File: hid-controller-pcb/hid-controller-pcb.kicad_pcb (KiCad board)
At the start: 2 copper layers, 120.2 x 66.8 mm, 64 parts, among them IC1 RT9080-33GJ5, J1 10118194-0011LF, J2 Jumper, U1 STM32F103C8Tx, U3 COM-09032, U4 COM-09032, Y1 8MHz, Y2 32.768KHz

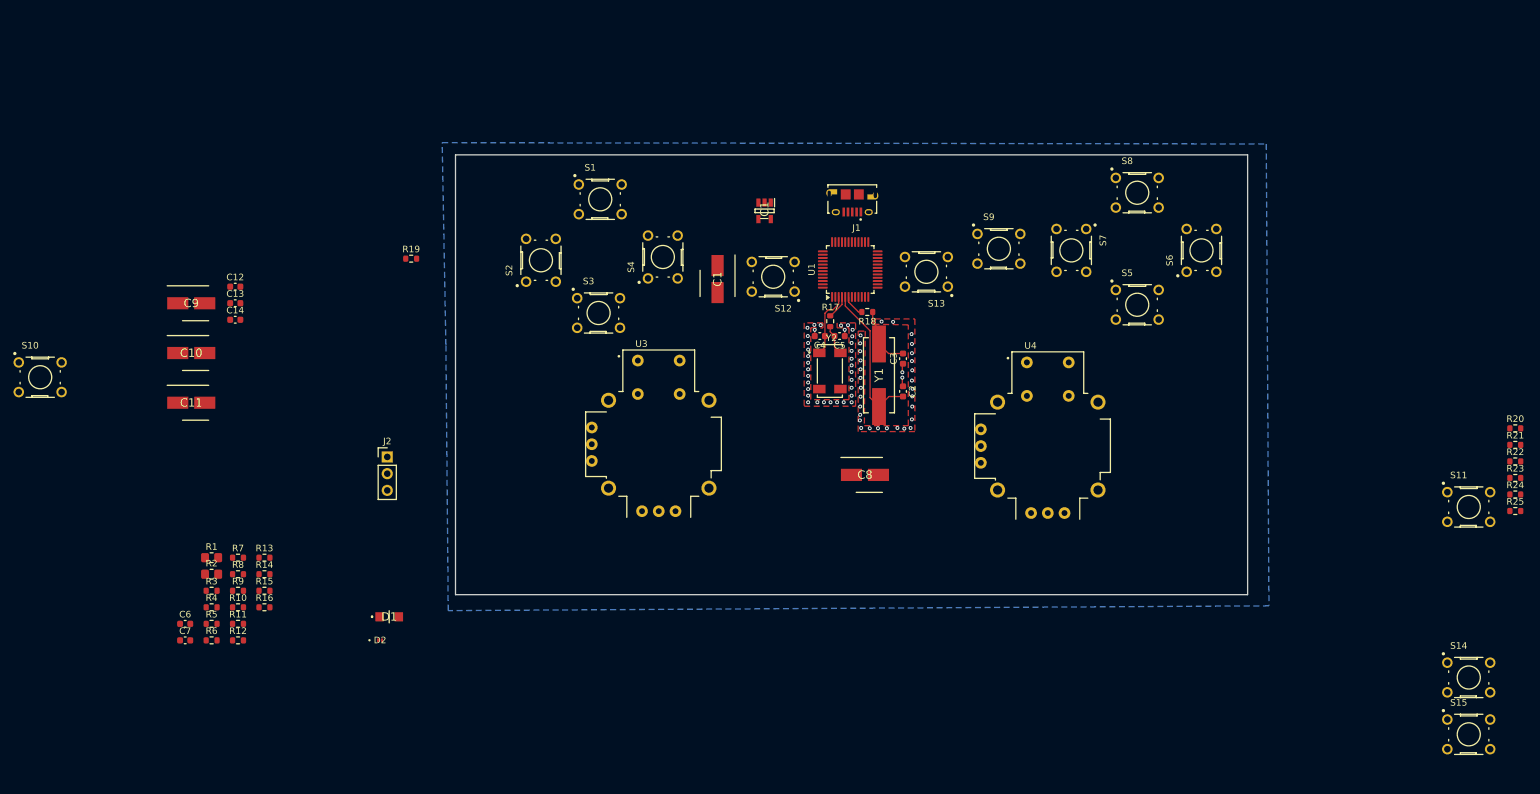
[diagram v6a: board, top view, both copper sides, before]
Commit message: working with xbox360ce remapping as a workaround for now, more work on the pcb
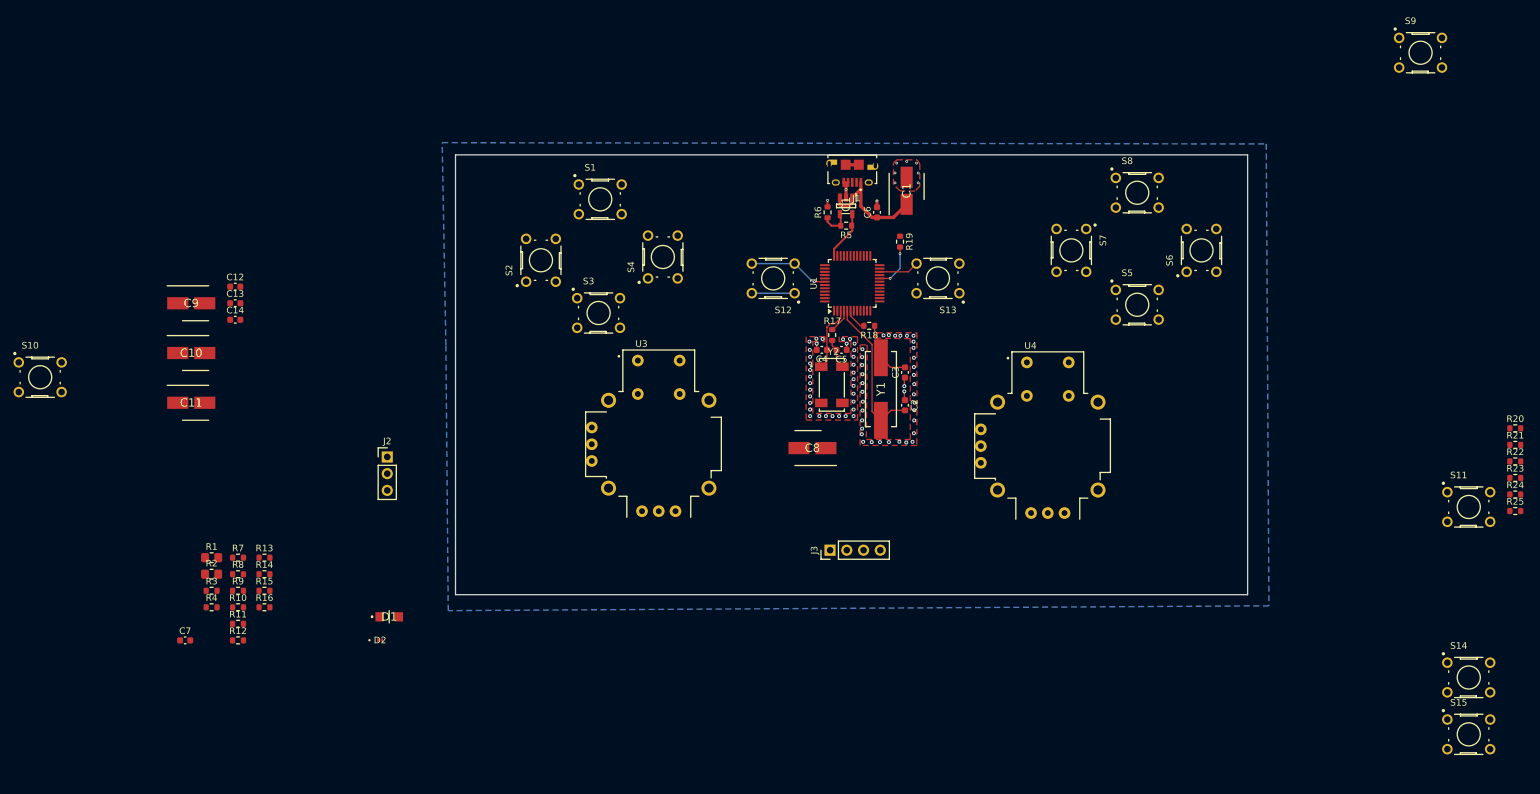
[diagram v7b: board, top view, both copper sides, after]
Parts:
- added J3: STLink, Connector_PinHeader_2.54mm:PinHeader_1x04_P2.54mm_Vertical, F.Cu at (203.9, 96.0)
- moved C6 122.2 mm to (211.0, 44.7), turned to 90 degrees
- moved R6 113.8 mm to (203.5, 44.7), turned to 90 degrees
- moved R5 113.7 mm to (206.3, 46.8), turned to 180 degrees
- moved R19 74.2 mm to (214.5, 49.2), turned to -90 degrees
- moved S9 70.6 mm to (293.5, 20.5)
- moved C1 31.7 mm to (215.5, 41.5), turned to 90 degrees
- moved IC1 12.4 mm to (206.3, 43.8)
- moved C8 8.96 mm to (201.2, 80.5), turned to 180 degrees
- moved J1 4.50 mm to (207.2, 37.5)
- moved C3 2.12 mm to (215.2, 69.0)
- moved Y2 2.12 mm to (204.2, 70.9)
- moved U1 2.12 mm to (207.2, 55.5)
- moved R17 2.12 mm to (204.2, 63.4)
- moved R18 2.12 mm to (209.8, 62.0)
- moved C2 2.12 mm to (215.2, 74.0)
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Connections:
- U1 pad 16: DPAD_1 -> AN_SEL2
- U1 pad 17: DPAD_2 -> BTN_2
- U1 pad 18: unconnected-(U1-PB0-Pad18) -> BTN_1
- U1 pad 19: unconnected-(U1-PB1-Pad19) -> BTN_3
- U1 pad 21: AN_SEL1 -> BTN_4
- U1 pad 22: AN_SEL2 -> BTN_STR
- U1 pad 25: BTN_SHR -> unconnected-(U1-PB12-Pad25)
- U1 pad 26: BTN_STR -> DPAD_1
- U1 pad 42: BTN_1 -> BTN_SHR
- U1 pad 43: BTN_2 -> DPAD_2
- U1 pad 45: BTN_3 -> AN_SEL1
- U1 pad 46: BTN_4 -> unconnected-(U1-PB9-Pad46)
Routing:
- net +5V: track 0.00 -> 17.9 mm
- net +3V3: track 0.00 -> 14.0 mm
- net BTN_SHR: track 0.00 -> 12.2 mm, vias 0 -> 1
- net BOOT1: track 0.00 -> 6.97 mm, vias 0 -> 2
- net GND: track 4.61 -> 11.5 mm, vias 66 -> 81
- net BTN_STR: track 0.00 -> 6.12 mm
- net Net-(IC1-SNS): track 0.00 -> 4.67 mm

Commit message: switched to 4 layer board, too many traces :(
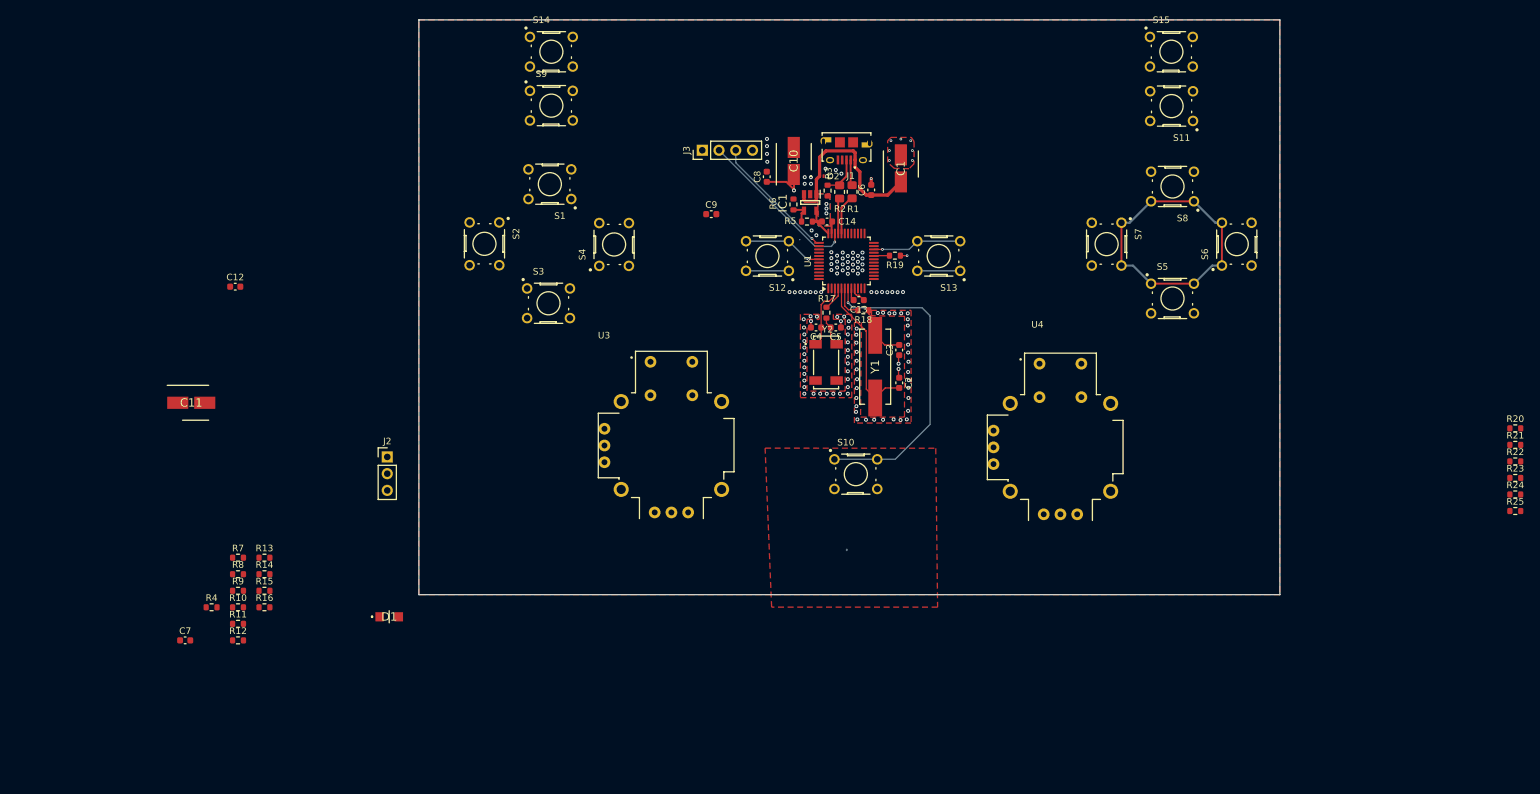
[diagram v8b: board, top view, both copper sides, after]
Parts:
- C8, C9: value 10uF -> 1uF; footprint lib:CAPAE530X550N -> Capacitor_SMD:C_0603_1608Metric
- moved S14 168.5 mm to (161.6, 20.4)
- moved S9 132.2 mm to (161.6, 28.5)
- moved S10 124.7 mm to (207.8, 84.5)
- moved S15 113.0 mm to (255.7, 20.4)
- moved R1 112.0 mm to (207.2, 41.6), turned to -90 degrees
- moved R2 111.6 mm to (205.3, 41.6), turned to -90 degrees
- moved R3 111.5 mm to (203.5, 41.4), turned to 90 degrees
- moved D2 97.2 mm to (202.6, 39.2)
- moved C10 96.0 mm to (198.4, 36.9), turned to 90 degrees
- moved C13 94.6 mm to (208.2, 58.0), turned to 180 degrees
- moved C14 91.0 mm to (203.4, 46.1)
- moved C9 80.1 mm to (185.8, 45.0)
- moved S11 75.7 mm to (255.7, 28.6), turned to 180 degrees
- moved J3 63.7 mm to (184.5, 35.3)
- moved C8 41.8 mm to (194.3, 39.3), turned to 90 degrees
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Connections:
- R3 pad 1: +5V -> +3V3
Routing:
- net +3V3: track 14.0 -> 76.9 mm, vias 0 -> 4
- net Net-(U1-NRST): track 0.00 -> 48.6 mm, vias 0 -> 1
- net SWDIO: track 0.00 -> 25.4 mm, vias 0 -> 1
- net SWCLK: track 0.00 -> 19.6 mm, vias 0 -> 1
- net +5V: track 17.9 -> 28.8 mm
- net BTN_STR: track 6.12 -> 13.6 mm, vias 0 -> 1
- net PA11: track 0.00 -> 6.12 mm
- net Net-(J1-D+): track 0.00 -> 6.12 mm
- net PA12: track 0.00 -> 5.46 mm
- net BOOT1: track 6.97 -> 2.40 mm, vias 2 -> 0
- net Net-(J1-D-): track 0.00 -> 3.93 mm
- net OSC_OUT: track 3.45 -> 4.94 mm
- net Net-(IC1-SNS): track 4.67 -> 3.46 mm
- net GND: track 11.5 -> 10.4 mm, vias 81 -> 135
- net Net-(C3-Pad2): track 9.49 -> 8.45 mm
- added copper zone on B.Cu, net +3V3
- added copper zone on F.Cu, net +3V3
- added copper zone on In2.Cu, net +3V3
- added copper zone on In1.Cu, net GND
- added copper zone on In2.Cu, net GND
- removed copper zone on B.Cu, net GND
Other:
- board size 120.2 x 66.8 mm -> 130.7 x 87.2 mm
- copper layers 2 -> 4
